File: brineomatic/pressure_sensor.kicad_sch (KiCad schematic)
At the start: 6 parts

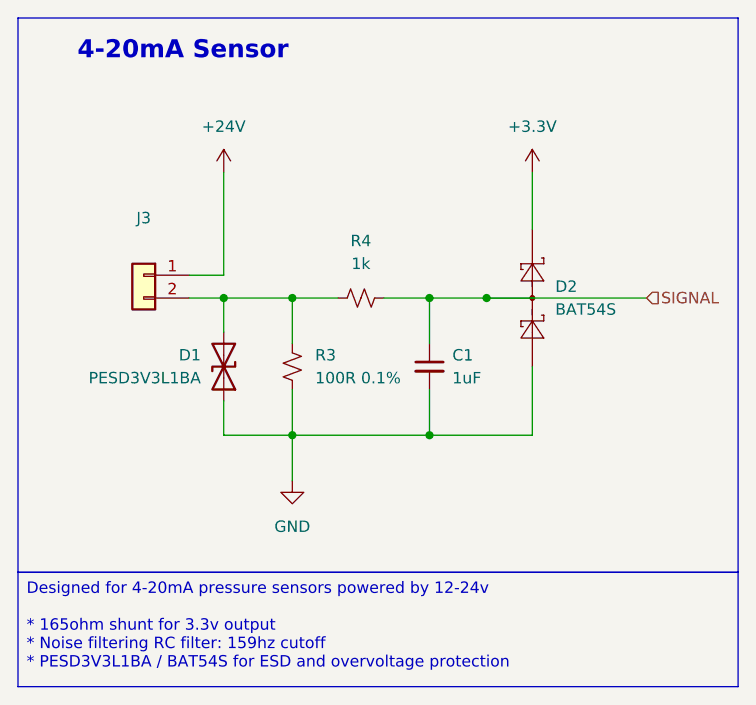
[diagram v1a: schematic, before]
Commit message: switched to bav199 on pressure / tds
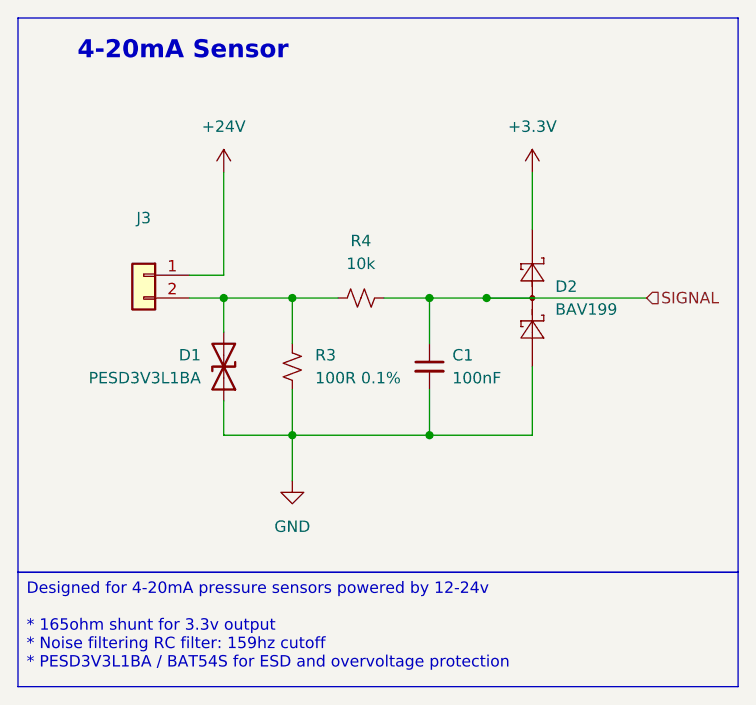
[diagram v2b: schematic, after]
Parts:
- C1: value 1uF -> 100nF
- D2: value BAT54S -> BAV199; LCSC C727126 -> C40919
- R4: value 1k -> 10k
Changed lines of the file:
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@@
 			)
 		)
-		(property "Value" "BAT54S"
+		(property "Value" "BAV199"
 			(at 138.43 88.9 90)
 			(effects
@@
 			)
 		)
-		(property "Datasheet" "https://www.diodes.com/assets/Datasheets/ds11005.pdf"
+		(property "Datasheet" "https://www.lcsc.com/datasheet/C40919.pdf"
 			(at 135.89 90.678 0)
 			(effects
@@
 			)
 		)
-		(property "LCSC" "C727126"
+		(property "LCSC" "C40919"
 			(at 135.89 87.63 90)
 			(effects
@@
 			)
 		)
-		(property "Value" "1k"
+		(property "Value" "10k"
 			(at 116.84 83.82 90)
 			(effects
@@
 			)
 		)
-		(property "Value" "1uF"
+		(property "Value" "100nF"
 			(at 127 96.5263 0)
 			(effects

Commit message: tested and update bom + placement
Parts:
- C1: LCSC (none) -> C14663
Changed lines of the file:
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@@
 			)
 		)
-		(property "LCSC" ""
+		(property "LCSC" "C14663"
 			(at 124.46 95.25 0)
 			(effects

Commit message: updated resistor p/ns in bom
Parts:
- R4: LCSC (none) -> C25804
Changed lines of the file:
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@@
 			)
 		)
-		(property "LCSC" ""
+		(property "LCSC" "C25804"
 			(at 116.84 87.63 0)
 			(effects

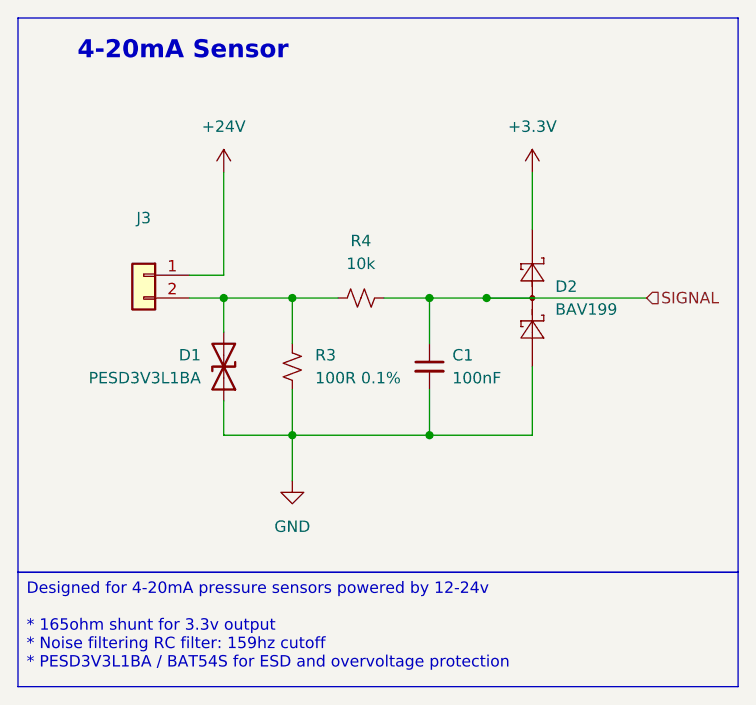
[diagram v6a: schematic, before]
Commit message: updated analog sensor esd schematic
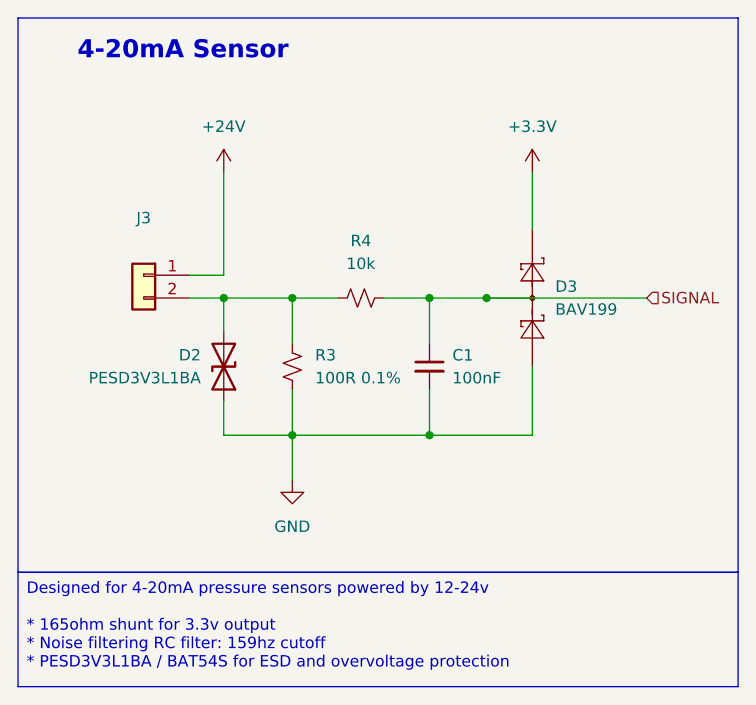
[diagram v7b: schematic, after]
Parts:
- renumbered D1 to D2, D2 to D3
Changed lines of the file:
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@@
 		(dnp no)
 		(fields_autoplaced yes)
-		(property "Reference" "#PWR09"
+		(property "Reference" "#PWR010"
 			(at 101.6 77.47 0)
 			(effects
@@
 			(project "brineomatic"
 				(path "/96477ae2-ef08-48f3-8dd4-fe4478541f68/c8ab4709-9ad5-4833-bb93-07e00d6a0170"
-					(reference "#PWR041")
-					(unit 1)
-				)
-				(path "/96477ae2-ef08-48f3-8dd4-fe4478541f68/e7fd98b0-0753-4e9e-b57d-135c0c1a0b39"
-					(reference "#PWR09")
+					(reference "#PWR042")
+					(unit 1)
+				)
+				(path "/96477ae2-ef08-48f3-8dd4-fe4478541f68/e7fd98b0-0753-4e9e-b57d-135c0c1a0b39"
+					(reference "#PWR010")
 					(unit 1)
 				)
@@
 		(dnp no)
 		(fields_autoplaced yes)
-		(property "Reference" "#PWR011"
+		(property "Reference" "#PWR012"
 			(at 135.89 77.47 0)
 			(effects
@@
 			(project "brineomatic"
 				(path "/96477ae2-ef08-48f3-8dd4-fe4478541f68/c8ab4709-9ad5-4833-bb93-07e00d6a0170"
-					(reference "#PWR043")
-					(unit 1)
-				)
-				(path "/96477ae2-ef08-48f3-8dd4-fe4478541f68/e7fd98b0-0753-4e9e-b57d-135c0c1a0b39"
-					(reference "#PWR011")
+					(reference "#PWR044")
+					(unit 1)
+				)
+				(path "/96477ae2-ef08-48f3-8dd4-fe4478541f68/e7fd98b0-0753-4e9e-b57d-135c0c1a0b39"
+					(reference "#PWR012")
 					(unit 1)
 				)
@@
 		(dnp no)
 		(fields_autoplaced yes)
-		(property "Reference" "#PWR010"
+		(property "Reference" "#PWR011"
 			(at 109.22 114.3 0)
 			(effects
@@
 			(project "brineomatic"
 				(path "/96477ae2-ef08-48f3-8dd4-fe4478541f68/c8ab4709-9ad5-4833-bb93-07e00d6a0170"
-					(reference "#PWR042")
-					(unit 1)
-				)
-				(path "/96477ae2-ef08-48f3-8dd4-fe4478541f68/e7fd98b0-0753-4e9e-b57d-135c0c1a0b39"
-					(reference "#PWR010")
+					(reference "#PWR043")
+					(unit 1)
+				)
+				(path "/96477ae2-ef08-48f3-8dd4-fe4478541f68/e7fd98b0-0753-4e9e-b57d-135c0c1a0b39"
+					(reference "#PWR011")
 					(unit 1)
 				)
@@
 		(dnp no)
 		(fields_autoplaced yes)
-		(property "Reference" "D2"
+		(property "Reference" "D3"
 			(at 138.43 86.36 90)
 			(effects
@@
 			(project "brineomatic"
 				(path "/96477ae2-ef08-48f3-8dd4-fe4478541f68/c8ab4709-9ad5-4833-bb93-07e00d6a0170"
-					(reference "D35")
-					(unit 1)
-				)
-				(path "/96477ae2-ef08-48f3-8dd4-fe4478541f68/e7fd98b0-0753-4e9e-b57d-135c0c1a0b39"
-					(reference "D2")
+					(reference "D36")
+					(unit 1)
+				)
+				(path "/96477ae2-ef08-48f3-8dd4-fe4478541f68/e7fd98b0-0753-4e9e-b57d-135c0c1a0b39"
+					(reference "D3")
 					(unit 1)
 				)
@@
 		(on_board yes)
 		(dnp no)
-		(property "Reference" "D1"
+		(property "Reference" "D2"
 			(at 99.06 93.9799 90)
 			(effects
@@
 			(project "brineomatic"
 				(path "/96477ae2-ef08-48f3-8dd4-fe4478541f68/c8ab4709-9ad5-4833-bb93-07e00d6a0170"
-					(reference "D34")
-					(unit 1)
-				)
-				(path "/96477ae2-ef08-48f3-8dd4-fe4478541f68/e7fd98b0-0753-4e9e-b57d-135c0c1a0b39"
-					(reference "D1")
-					(unit 1)
-				)
+					(reference "D35")
+					(unit 1)
+				)
+				(path "/96477ae2-ef08-48f3-8dd4-fe4478541f68/e7fd98b0-0753-4e9e-b57d-135c0c1a0b39"
+					(reference "D2")
+					(unit 1)
+				)

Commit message: added bulk cap after ideal diode
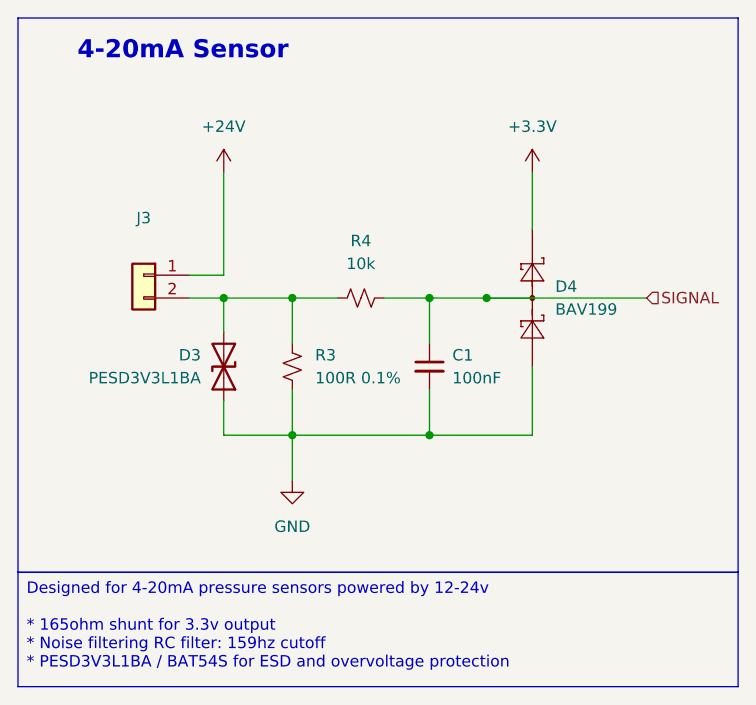
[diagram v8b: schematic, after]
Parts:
- renumbered D2 to D3, D3 to D4
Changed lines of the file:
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@@
 		(dnp no)
 		(fields_autoplaced yes)
-		(property "Reference" "#PWR010"
+		(property "Reference" "#PWR012"
 			(at 101.6 77.47 0)
 			(effects
@@
 			(project "brineomatic"
 				(path "/96477ae2-ef08-48f3-8dd4-fe4478541f68/c8ab4709-9ad5-4833-bb93-07e00d6a0170"
-					(reference "#PWR042")
+					(reference "#PWR044")
 					(unit 1)
 				)
 				(path "/96477ae2-ef08-48f3-8dd4-fe4478541f68/e7fd98b0-0753-4e9e-b57d-135c0c1a0b39"
-					(reference "#PWR010")
+					(reference "#PWR012")
 					(unit 1)
 				)
@@
 		(dnp no)
 		(fields_autoplaced yes)
-		(property "Reference" "#PWR012"
+		(property "Reference" "#PWR014"
 			(at 135.89 77.47 0)
 			(effects
@@
 			(project "brineomatic"
 				(path "/96477ae2-ef08-48f3-8dd4-fe4478541f68/c8ab4709-9ad5-4833-bb93-07e00d6a0170"
-					(reference "#PWR044")
+					(reference "#PWR046")
 					(unit 1)
 				)
 				(path "/96477ae2-ef08-48f3-8dd4-fe4478541f68/e7fd98b0-0753-4e9e-b57d-135c0c1a0b39"
-					(reference "#PWR012")
+					(reference "#PWR014")
 					(unit 1)
 				)
@@
 		(dnp no)
 		(fields_autoplaced yes)
-		(property "Reference" "#PWR011"
+		(property "Reference" "#PWR013"
 			(at 109.22 114.3 0)
 			(effects
@@
 			(project "brineomatic"
 				(path "/96477ae2-ef08-48f3-8dd4-fe4478541f68/c8ab4709-9ad5-4833-bb93-07e00d6a0170"
-					(reference "#PWR043")
+					(reference "#PWR045")
 					(unit 1)
 				)
 				(path "/96477ae2-ef08-48f3-8dd4-fe4478541f68/e7fd98b0-0753-4e9e-b57d-135c0c1a0b39"
-					(reference "#PWR011")
+					(reference "#PWR013")
 					(unit 1)
 				)
@@
 		(dnp no)
 		(fields_autoplaced yes)
-		(property "Reference" "D3"
+		(property "Reference" "D4"
 			(at 138.43 86.36 90)
 			(effects
@@
 			(project "brineomatic"
 				(path "/96477ae2-ef08-48f3-8dd4-fe4478541f68/c8ab4709-9ad5-4833-bb93-07e00d6a0170"
-					(reference "D36")
+					(reference "D35")
 					(unit 1)
 				)
 				(path "/96477ae2-ef08-48f3-8dd4-fe4478541f68/e7fd98b0-0753-4e9e-b57d-135c0c1a0b39"
-					(reference "D3")
+					(reference "D4")
 					(unit 1)
 				)
@@
 		(on_board yes)
 		(dnp no)
-		(property "Reference" "D2"
+		(property "Reference" "D3"
 			(at 99.06 93.9799 90)
 			(effects
@@
 			(project "brineomatic"
 				(path "/96477ae2-ef08-48f3-8dd4-fe4478541f68/c8ab4709-9ad5-4833-bb93-07e00d6a0170"
-					(reference "D35")
+					(reference "D34")
 					(unit 1)
 				)
 				(path "/96477ae2-ef08-48f3-8dd4-fe4478541f68/e7fd98b0-0753-4e9e-b57d-135c0c1a0b39"
-					(reference "D2")
+					(reference "D3")
 					(unit 1)
 				)
@@
 			(project "brineomatic"
 				(path "/96477ae2-ef08-48f3-8dd4-fe4478541f68/c8ab4709-9ad5-4833-bb93-07e00d6a0170"
-					(reference "C25")
-					(unit 1)
-				)
+					(reference "C27")
+					(unit 1)
+				)
